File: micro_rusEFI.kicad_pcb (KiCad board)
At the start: 4 copper layers, 80.6 x 93.7 mm, 257 parts, among them J1 UJ20-C-V-C-2-SMT-TR, J12 Conn_01x01, J13 Conn_01x01, J15 Conn_01x01, J17 Conn_01x01, J19 Conn_01x06, J2 Conn_02x05_Odd_Even, J3 Conn_01x01, J4 Conn_02x05_Counter_Clockwise, J5 Conn_01x01, J6 Micro_SD_Card_Det, J7 TC2030, Q1 IPD30N06S2L-23, SW1 SW_Push, SW2 SW_Push, SW3 SW_Push, SW4 SW_Push, U1 STM32F427VGT6, U10 VNLD5090, U2 TLE8888QK, U3 molex_48pin_MRE, U31 MIC4427, U32 MIC4427, U33 MIC4427, U35 MCP6004, U36 MCP6004, U4 TLE9201SG, U46 MCP6004, U5 LM1117-3.3, U7 XC6206 3.3V, U8 MCP6004, U9 VNLD5090, X1 8MHz 20pF, Y2 32768 Hz

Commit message: completed board, created BOM
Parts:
- added G***: LOGO, Raccoon_Logo:Raccoon Logo, B.Cu at (61.3, 71.9)
- C39: footprint Capacitor_SMD:C_0603_1608Metric -> Capacitor_SMD:C_0805_2012Metric
- moved NT3 11.8 mm to (57.7, 85.1)
- moved R87 1.17 mm to (58.0, 107.5)
- moved C39 0.55 mm to (27.0, 102.3)
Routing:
- net /ADC/AGND: track 27.3 -> 14.1 mm, vias 3 -> 15
- net GND: track 119.2 -> 115.4 mm, vias 511 -> 514
- net /12V_MREL: track 229.9 -> 231.7 mm
- net /MCU/shield: track 16.3 -> 14.6 mm, vias 0 -> 4
- net /MCU/Vbus: track 59.8 -> 61.0 mm, vias 3 -> 2
- net /RST: track 107.4 -> 108.6 mm
- net Net-(J1-CC1): track 3.86 -> 4.76 mm
- net Net-(U8D--): track 6.30 -> 5.63 mm
- net /AT3_MCU: track 29.3 -> 28.7 mm
- net /AT4_MCU: track 28.7 -> 28.2 mm
- net /12V_SAFE: track 140.7 -> 140.6 mm, vias 57 -> 56
- net /MCU/BOOT0: vias 1 -> 0
- added copper zone on In1.Cu, net /ADC/AGND
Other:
- board text added: "PA10 (USB_ID) PULL-DOWN"
- board text added: "R0.1 PCB DESIGN BY OLA RUUD R0.2 PCB DESIGN BY DAECU R0.3 PCB DESIGN BY DAECU R0.4 PCB DESIGN BY DBECKER R0.5 PCB DESIGN BY COMMUNITY USB-C PCB DESIGN BY RACOONDOEGGS"
- board text added: "microRusEFI R0.6.1"
- board text removed: "PA10 PULL-DOWN"
- board text removed: "R0.1 PCB DESIGN BY OLA RUUD R0.2 PCB DESIGN BY DAECU R0.3 PCB DESIGN BY DAECU R0.4 PCB DESIGN BY DBECKER R0.5 PCB DESIGN BY COMMUNITY"
- board text removed: "microRusEFI R0.6.0"

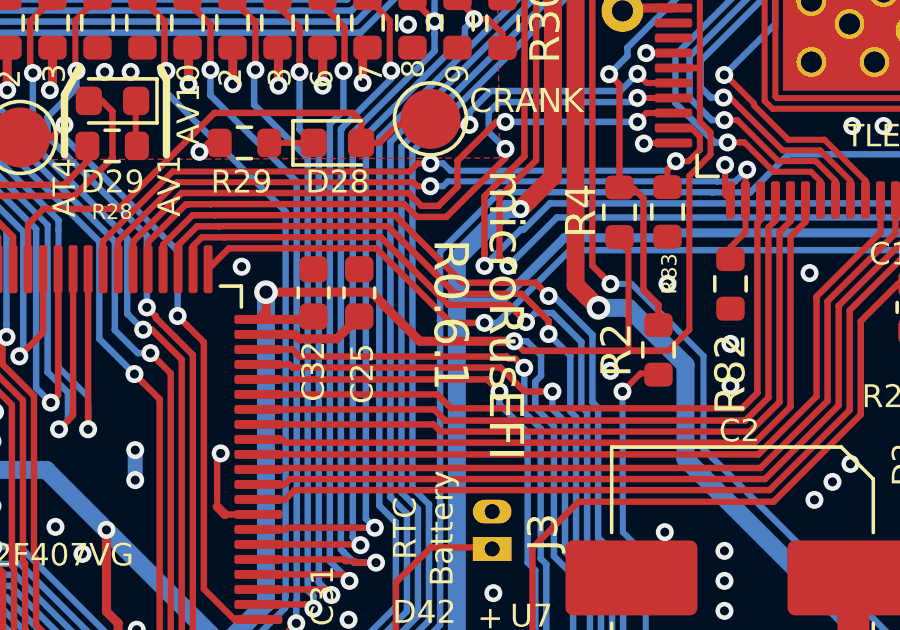
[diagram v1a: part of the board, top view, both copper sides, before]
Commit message: adjusted BOM and created production files
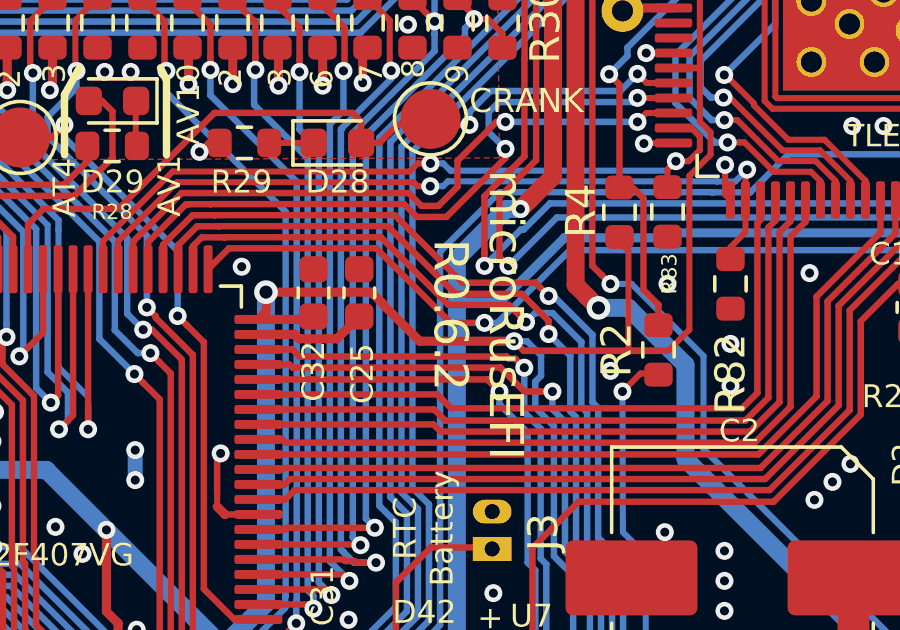
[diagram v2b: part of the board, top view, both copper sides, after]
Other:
- board text added: "R0.1 PCB DESIGN BY OLA RUUD R0.2 PCB DESIGN BY DAECU R0.3 PCB DESIGN BY DAECU R0.4 PCB DESIGN BY DBECKER R0.5 PCB DESIGN BY COMMUNITY R0.6.2 PCB DESIGN BY RACOONDOEGGS"
- board text added: "microRusEFI R0.6.2"
- board text removed: "R0.1 PCB DESIGN BY OLA RUUD R0.2 PCB DESIGN BY DAECU R0.3 PCB DESIGN BY DAECU R0.4 PCB DESIGN BY DBECKER R0.5 PCB DESIGN BY COMMUNITY USB-C PCB DESIGN BY RACOONDOEGGS"
- board text removed: "microRusEFI R0.6.1"
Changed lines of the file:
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@@
 		)
 	)
-	(gr_text "microRusEFI\nR0.6.1"
+	(gr_text "microRusEFI\nR0.6.2"
 		(at 69.088 80.137 270)
 		(layer "F.SilkS")
@@
 		)
 	)
-	(gr_text "R0.1 PCB DESIGN BY OLA RUUD\nR0.2 PCB DESIGN BY DAECU\nR0.3 PCB DESIGN BY DAECU\nR0.4 PCB DESIGN BY DBECKER\nR0.5 PCB DESIGN BY COMMUNITY\n\nUSB-C PCB DESIGN BY RACOONDOEGGS"
+	(gr_text "R0.1 PCB DESIGN BY OLA RUUD\nR0.2 PCB DESIGN BY DAECU\nR0.3 PCB DESIGN BY DAECU\nR0.4 PCB DESIGN BY DBECKER\nR0.5 PCB DESIGN BY COMMUNITY\n\nR0.6.2 PCB DESIGN BY RACOONDOEGGS"
 		(at 21.336 64.3636 0)
 		(layer "B.SilkS")
@@
 		)
 	)
-	(gr_text "microRusEFI\nR0.6.1"
+	(gr_text "microRusEFI\nR0.6.2"
 		(at 90.805 51.435 0)
 		(layer "B.SilkS")
